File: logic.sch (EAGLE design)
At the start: 86 parts, among them CON11 PINHEAD_1X03-2, CON12 PINHEAD_1X03-2, CON2 PINHEAD_2X02-PTH-2-MALE, CON3 PINHEAD_2X04-PLS-2, CON4 CON-3P-TABS, CON5 PINHEAD_2X02-PTH-2-MALE, CON6 PINHEAD_2X02-PTH-2-MALE, CON7 PINHEAD_2X02-PTH-2-MALE, IC1 STM32F105RCT6, IC10 LM75-TSSOP8, IC11 LM75-TSSOP8, IC2 CAT24C02, IC3 NCV8603SN33, IC4 TPS62160QDSGRQ1, IC6 ZXCT1051, IC7 ST3232, IC8 LM75-TSSOP8, IC9 LM5008-MSOP8, X1 24MHz

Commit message: attribute updates
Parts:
- D8: LCSC# (none) -> C475665
- IC1: LCSC# (none) -> C8345
- IC10, IC11, IC8: LCSC# (none) -> C33099
- IC2: LCSC# (none) -> C81340
- IC3: value NCV8603SN33 -> AP2127-3.3; device linear regulators:NCV8603SN33 -> linear regulators:AP2127-3.3; LCSC# (none) -> C156285
- IC4: LCSC# (none) -> C324077
- IC7: LCSC# (none) -> C435947
- IC9: LCSC# (none) -> C9424
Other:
- note added: "LED1 should be replaced with this one https://lcsc.com/product-detail/Light-Emitting-Diodes-LED_FM-B2020RGBA-HG_C108793.html/?href=jlc-SMT"
- moved on the sheet: C11, C13, C22, C25, C28, C29, C30, CON2, CON3, CON5, CON6, CON7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

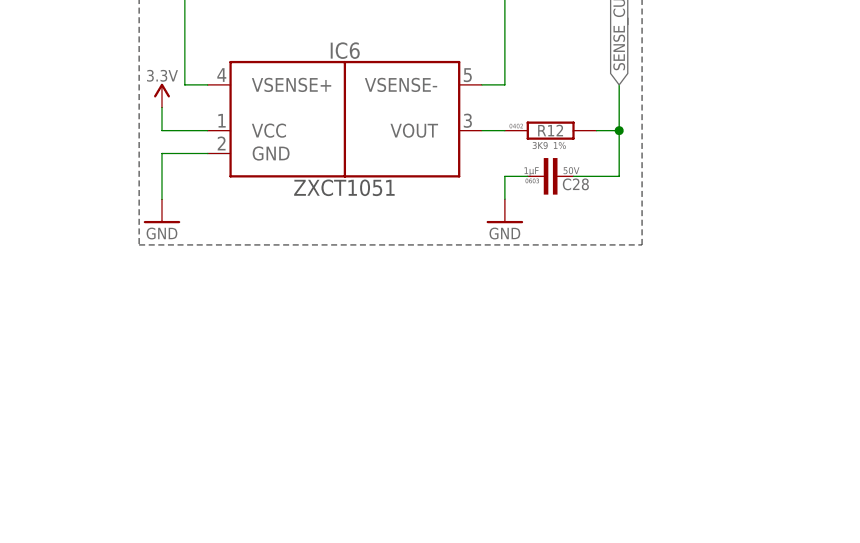
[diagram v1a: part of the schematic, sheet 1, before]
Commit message: Update logic.sch
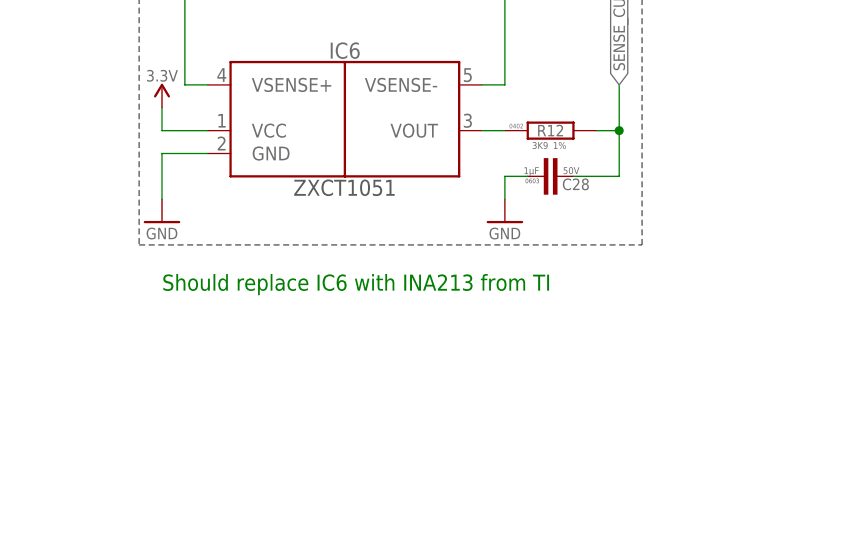
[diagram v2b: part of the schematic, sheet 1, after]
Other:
- note added: "Should replace IC6 with INA213 from TI"
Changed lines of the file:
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@@
 <text x="132.08" y="76.2" size="1.778" layer="91">LED1 should be replaced with this one
 https://lcsc.com/product-detail/Light-Emitting-Diodes-LED_FM-B2020RGBA-HG_C108793.html/?href=jlc-SMT</text>
+<text x="241.3" y="30.48" size="1.778" layer="91">Should replace IC6 with INA213 from TI</text>
 </plain>
 <instances>

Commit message: Power supply scheme rearrangement
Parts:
- removed C12, C14, C15, C24: 10uF, rc:C-0805
- removed C16: 0.47uF, rc:C-0402
- removed C35: 1uF, rc:C-1206
- removed C36: 0.1uF, rc:C-0805
- removed C43: 0.01uF, rc:C-0402
- removed D8: DFLS1100, Diodes:DFLS1100
- removed IC4: TPS62160QDSGRQ1, dc-dc:TPS62160QDSGRQ1
- removed IC9: LM5008-MSOP8, dc-dc:LM5008-MSOP8
- removed L1: 2.2µH, power_inductors:2.2µH-NRS3015
- removed L3, L4: 100µH, power_inductors:100µH-LQS-6028
- removed R1, R14: 51K, rc:R-1%-0402
- removed R13, R6: 2R, rc:R-1%-0805
- removed R18, R5: 10K, rc:R-1%-0402
- removed R20: 287K, rc:R-1%-0402
- removed R21: 143K, rc:R-1%-0402
- X1: value 24MHz -> 16MHz; device crystal:CRYSTAL-4P-24MHZ-3.2X2.5-4P -> crystal:CRYSTAL-4P-16MHZ-2.0X1.6
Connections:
- removed net N$15: L4.2, R1.2, R6.2
- removed net N$4: IC4.SW, L1.1
- removed net N$5: C16.2, IC9.VCC
- removed net N$50: IC9.FB, R1.1, R5.2
- removed net N$8: IC9.RT/SD, R20.1
- removed net N$9: IC4.FB, R14.1, R18.2
- removed net VDD_15V: C15.2, C24.2, IC4.EN, IC4.VIN, R6.1
- new net IN: C1.2, C2.2, IC1.EN, IC1.VIN, R2.1, R3.2
- new net OUT: C2.2, C3.2, C4.2, D1.A, IC1.VOS
- net GND: now also C2.1, IC1.AGND, IC1.FB, IC1.PGND; no longer C12.1, C14.1, C15.1, C16.1, C24.1, C35.1, C36.1, D8.A, IC4.AGND, IC4.PGND, IC9.RTN, R18.1, R21.1, R5.1
- net N$1: now also IC1.SW
- net N$10: now also C5.2, D1.C, IC1.VCC; no longer C35.2, C36.2, IC9.VIN, R13.1, R20.2
- net N$11: now also IC1.RON, R2.2; no longer C43.1, IC9.BST
- net N$12: now also C3.1, IC1.BST
- net N$13: now also C3.2, IC1.SW; no longer IC9.RCL, R21.2
- net N$14: now also IC1.FB; no longer C43.2, D8.C, IC9.SW, L3.1
- net N$17: now also IC1.UVLO, R3.1, R4.2; no longer L3.2, L4.1
- net VBAT: no longer R13.2
- net VDD_5V: no longer C12.2, C14.2, IC4.VOS, L1.2, R14.2
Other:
- note removed: "Due to space constraints one bigger inductor is replaced with two series inductors L3 and L4, which will give total ~200uH"
- note removed: "F=383.6 KHz"
- note removed: "F=Vout/(1.385 * 10^(-10) * Rt)"
- note removed: "Fmax = Vout/(Vin_max * 400nS) = 401315.7895"
- note removed: "For more detailed calculations on Rt and Rcl resistors refer to the spreadsheet linked in schematic description"
- note removed: "Imin = 610mA"
- note removed: "Lmin = 167 uH"
- note removed: "Lmin = Vout*(Vin-Vout)/(Ior*F*Vin)"
- note removed: "R23 = 51K"
- note removed: "R24 = 10K"
- note removed: "Vin_max = 95V"
- note removed: "Vout = 15.25V"
- note removed: "Vout = 2.5(R24+R23)/R24"
- moved on the sheet: C17, C18, C19, C20, C21, C23, C26, C27, IC3

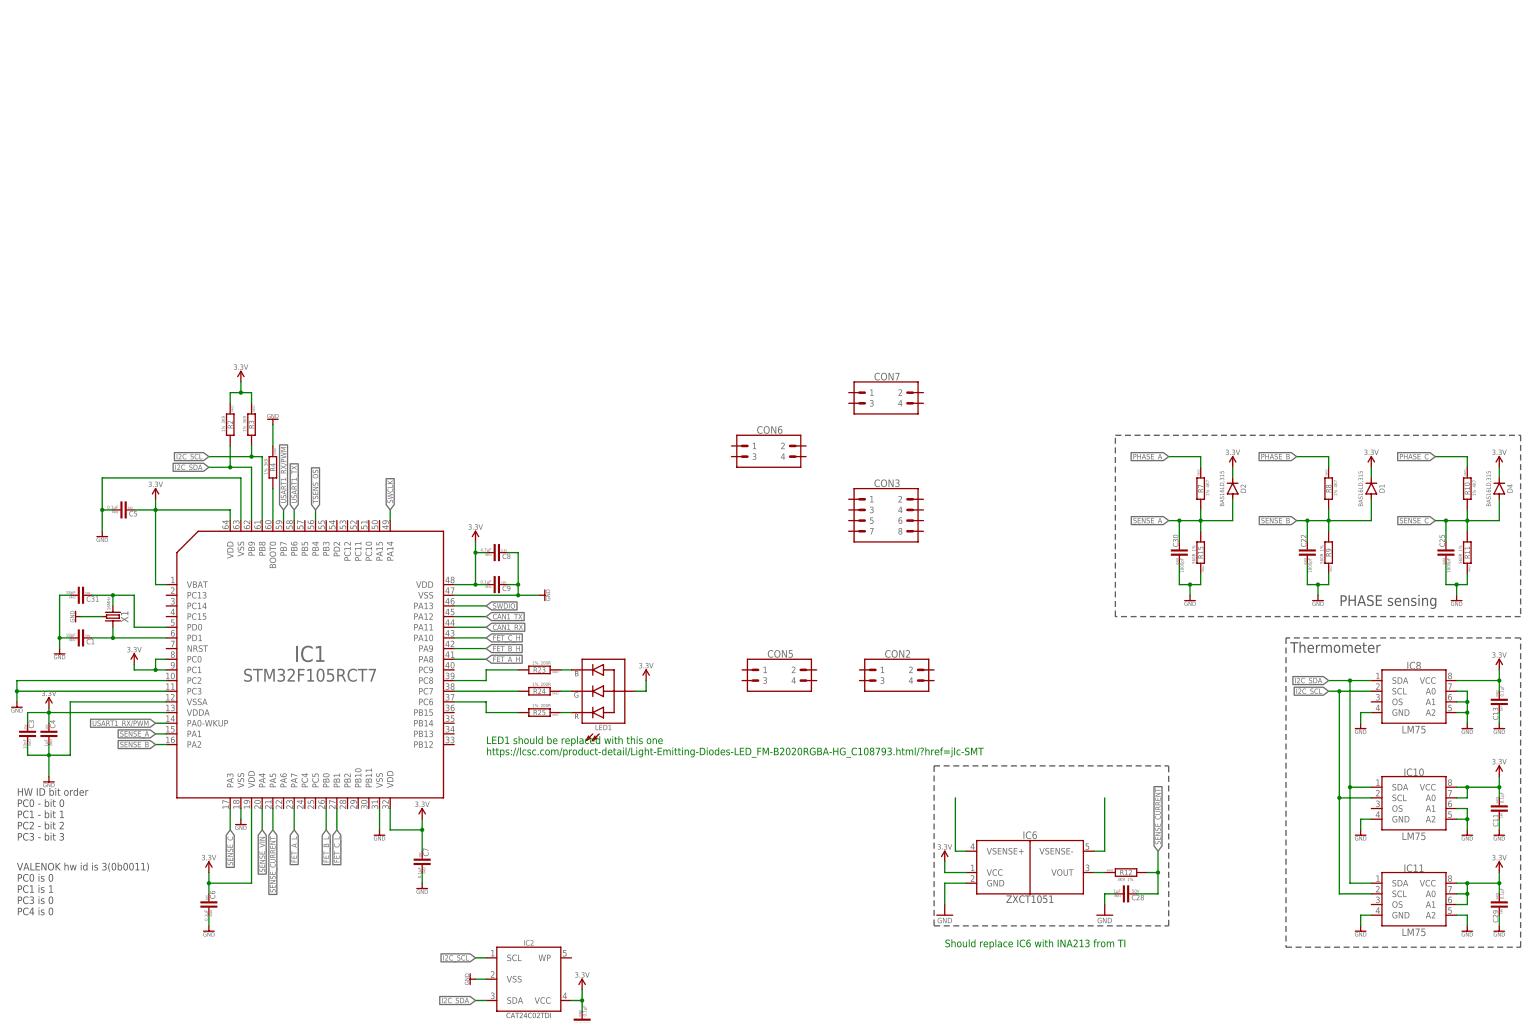
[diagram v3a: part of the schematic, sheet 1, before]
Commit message: HV dc-dc update
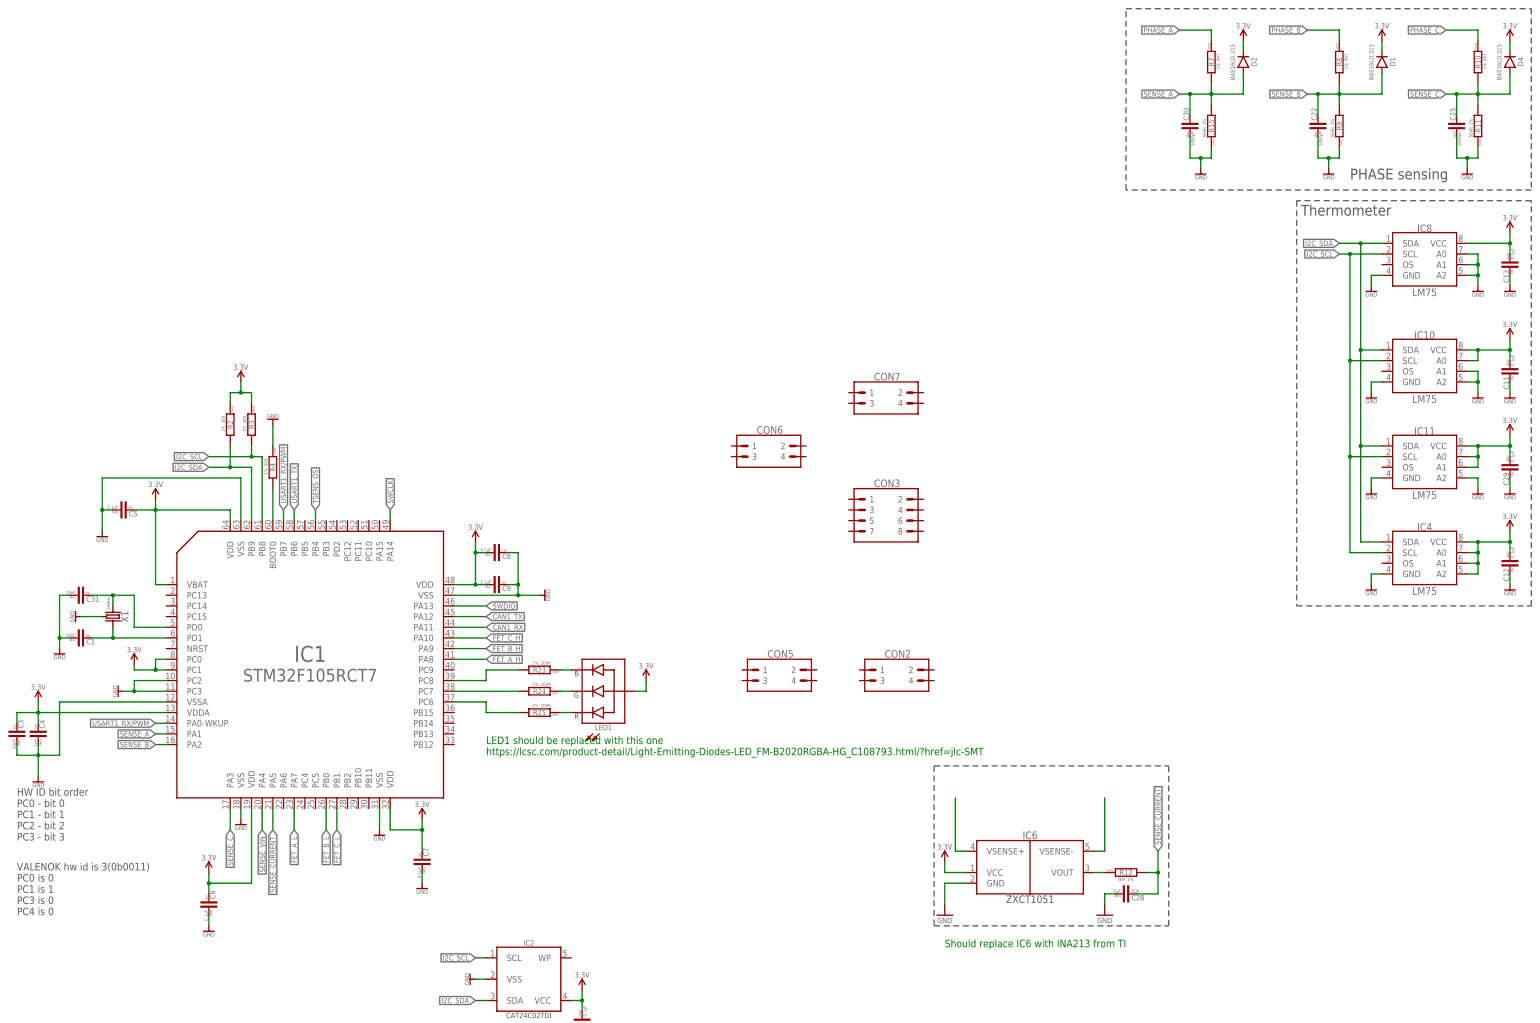
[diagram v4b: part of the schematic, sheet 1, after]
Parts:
- added C12: 0.1µF, rc:C-0402
- added IC4: LM75-TSSOP8, misc:LM75-TSSOP8
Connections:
- removed net N$13: C3.2, IC1.SW
- net GND: now also C12.2, IC1.RTN, IC4.GND
- net I2C_SCL: now also IC4.SCL
- net I2C_SDA: now also IC4.SDA
- net IN: no longer R2.1
- net N$11: no longer R2.2
- net N$2: now also C3.2, IC1.SW
- net VDD_3V3: now also C12.1, IC4.A0, IC4.A1, IC4.A2, IC4.VCC
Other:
- note added: "Alternate inductor may be used with the same footprint. 1264EY-101M=P3 from Murata Electronics. https://www.digikey.com/en/products/detail/murata-electronics/1264EY-101M=P3/5271456"
- moved on the sheet: C11, C13, C2, C22, C25, C29, C3, C30, C32, C33, C34, C37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
